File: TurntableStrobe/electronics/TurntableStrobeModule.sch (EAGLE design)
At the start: 11 parts, among them IC1 TINY25, J1 ISP, Q1 12MHz

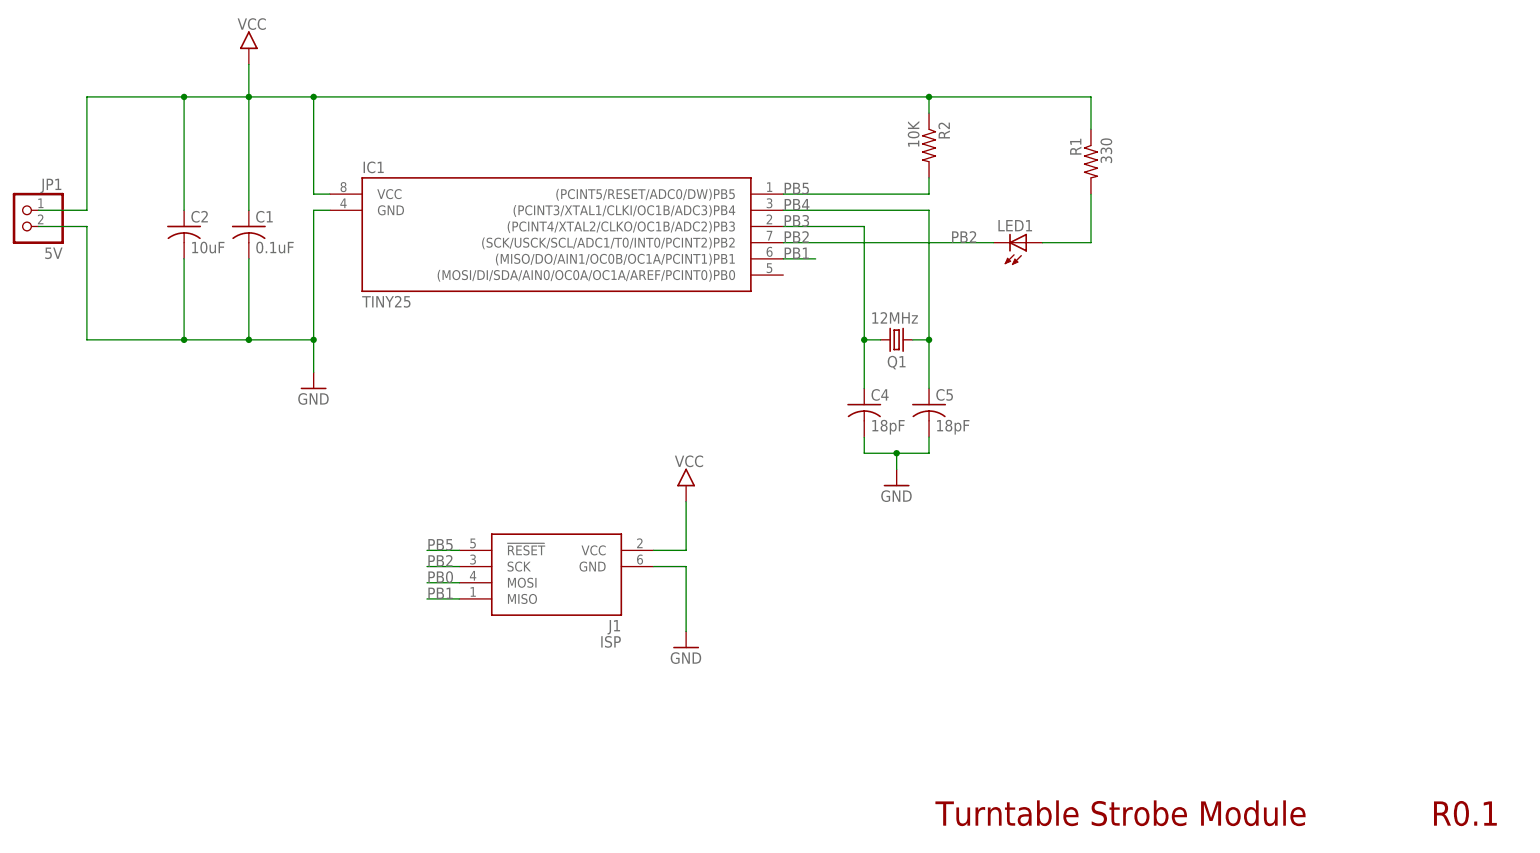
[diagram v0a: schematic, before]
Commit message: Fixed bug with missing MOSI.
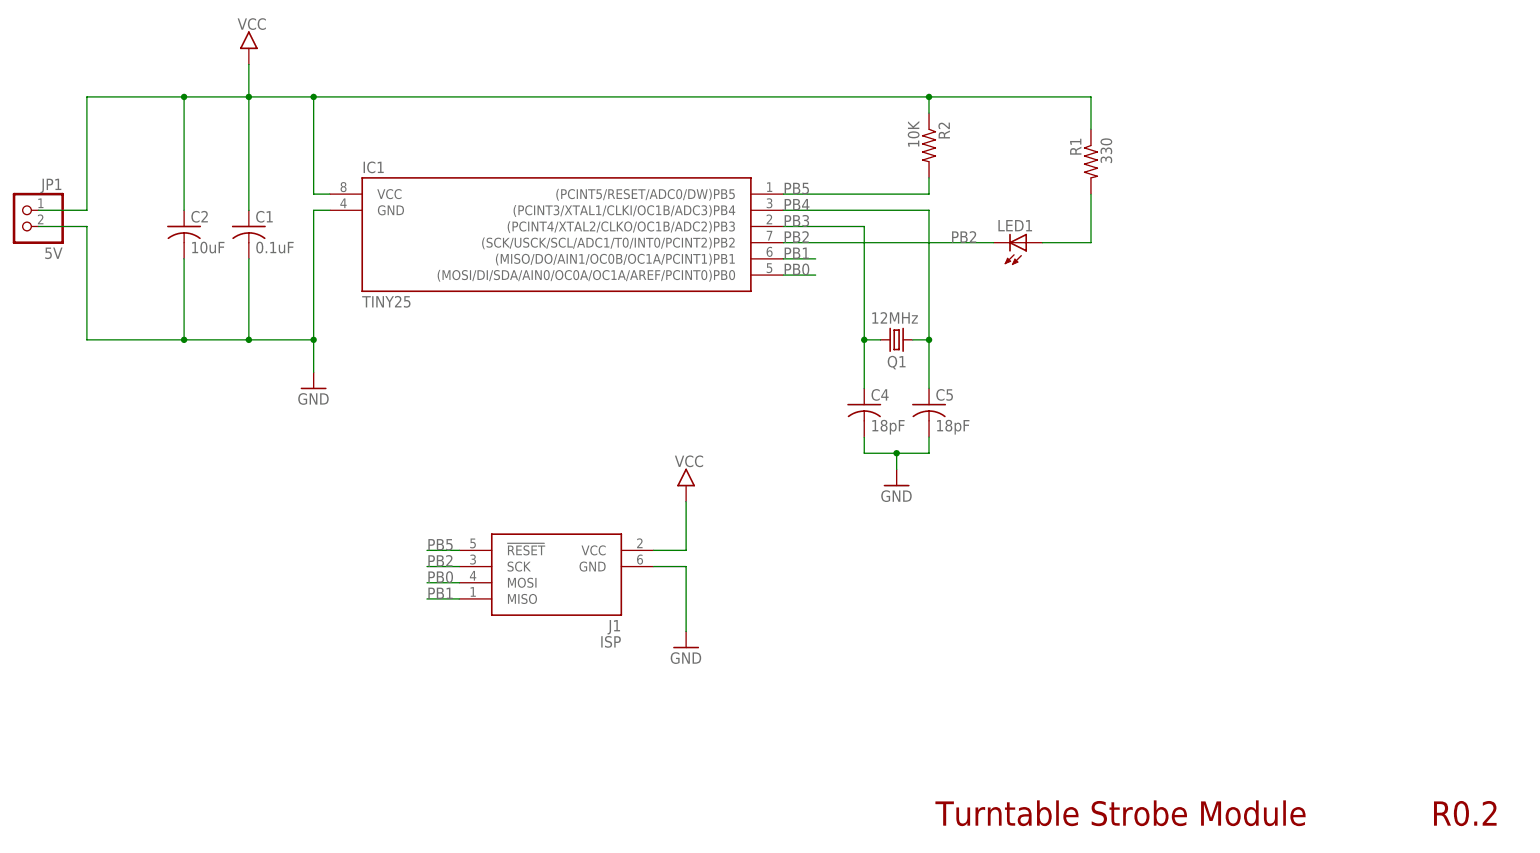
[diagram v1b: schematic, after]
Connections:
- net PB0: now also IC1.(MOSI/DI/SDA/AIN0/OC0A/OC1A/AREF/PCINT0)PB0
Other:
- note added: "R0.2"
- note removed: "R0.1"
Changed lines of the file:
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@@
 <grid distance="0.1" unitdist="inch" unit="inch" style="lines" multiple="1" display="no" altdistance="0.01" altunitdist="inch" altunit="inch"/>
 <layers>
-<layer number="1" name="Top" color="4" fill="1" visible="yes" active="no"/>
-<layer number="16" name="Bottom" color="1" fill="1" visible="yes" active="no"/>
-<layer number="17" name="Pads" color="2" fill="1" visible="yes" active="no"/>
-<layer number="18" name="Vias" color="2" fill="1" visible="yes" active="no"/>
-<layer number="19" name="Unrouted" color="6" fill="1" visible="yes" active="no"/>
-<layer number="20" name="Dimension" color="15" fill="1" visible="yes" active="no"/>
-<layer number="21" name="tPlace" color="7" fill="1" visible="yes" active="no"/>
-<layer number="22" name="bPlace" color="7" fill="1" visible="yes" active="no"/>
-<layer number="23" name="tOrigins" color="15" fill="1" visible="yes" active="no"/>
-<layer number="24" name="bOrigins" color="15" fill="1" visible="yes" active="no"/>
-<layer number="25" name="tNames" color="7" fill="1" visible="yes" active="no"/>
-<layer number="26" name="bNames" color="7" fill="1" visible="yes" active="no"/>
-<layer number="27" name="tValues" color="7" fill="1" visible="yes" active="no"/>
-<layer number="28" name="bValues" color="7" fill="1" visible="yes" active="no"/>
+<layer number="1" name="Top" color="4" fill="1" visible="no" active="no"/>
+<layer number="16" name="Bottom" color="1" fill="1" visible="no" active="no"/>
+<layer number="17" name="Pads" color="2" fill="1" visible="no" active="no"/>
+<layer number="18" name="Vias" color="2" fill="1" visible="no" active="no"/>
+<layer number="19" name="Unrouted" color="6" fill="1" visible="no" active="no"/>
+<layer number="20" name="Dimension" color="15" fill="1" visible="no" active="no"/>
+<layer number="21" name="tPlace" color="7" fill="1" visible="no" active="no"/>
+<layer number="22" name="bPlace" color="7" fill="1" visible="no" active="no"/>
+<layer number="23" name="tOrigins" color="15" fill="1" visible="no" active="no"/>
+<layer number="24" name="bOrigins" color="15" fill="1" visible="no" active="no"/>
+<layer number="25" name="tNames" color="7" fill="1" visible="no" active="no"/>
+<layer number="26" name="bNames" color="7" fill="1" visible="no" active="no"/>
+<layer number="27" name="tValues" color="7" fill="1" visible="no" active="no"/>
+<layer number="28" name="bValues" color="7" fill="1" visible="no" active="no"/>
 <layer number="29" name="tStop" color="7" fill="3" visible="no" active="no"/>
 <layer number="30" name="bStop" color="7" fill="6" visible="no" active="no"/>
@@
 <layer number="35" name="tGlue" color="7" fill="4" visible="no" active="no"/>
 <layer number="36" name="bGlue" color="7" fill="5" visible="no" active="no"/>
-<layer number="37" name="tTest" color="7" fill="1" visible="yes" active="no"/>
-<layer number="38" name="bTest" color="7" fill="1" visible="yes" active="no"/>
+<layer number="37" name="tTest" color="7" fill="1" visible="no" active="no"/>
+<layer number="38" name="bTest" color="7" fill="1" visible="no" active="no"/>
 <layer number="39" name="tKeepout" color="4" fill="11" visible="no" active="no"/>
 <layer number="40" name="bKeepout" color="1" fill="11" visible="no" active="no"/>
@@
 <layer number="44" name="Drills" color="7" fill="1" visible="no" active="no"/>
 <layer number="45" name="Holes" color="7" fill="1" visible="no" active="no"/>
-<layer number="46" name="Milling" color="3" fill="1" visible="yes" active="no"/>
-<layer number="47" name="Measures" color="7" fill="1" visible="yes" active="no"/>
-<layer number="48" name="Document" color="7" fill="1" visible="yes" active="no"/>
-<layer number="49" name="Reference" color="7" fill="1" visible="yes" active="no"/>
-<layer number="50" name="dxf" color="7" fill="1" visible="yes" active="no"/>
-<layer number="51" name="tDocu" color="7" fill="1" visible="yes" active="no"/>
-<layer number="52" name="bDocu" color="7" fill="1" visible="yes" active="no"/>
-<layer number="53" name="tPadExt" color="7" fill="1" visible="yes" active="no"/>
-<layer number="54" name="bPadExt" color="1" fill="1" visible="yes" active="no"/>
-<layer number="56" name="wert" color="7" fill="1" visible="yes" active="no"/>
+<layer number="46" name="Milling" color="3" fill="1" visible="no" active="no"/>
+<layer number="47" name="Measures" color="7" fill="1" visible="no" active="no"/>
+<layer number="48" name="Document" color="7" fill="1" visible="no" active="no"/>
+<layer number="49" name="Reference" color="7" fill="1" visible="no" active="no"/>
+<layer number="50" name="dxf" color="7" fill="1" visible="no" active="no"/>
+<layer number="51" name="tDocu" color="7" fill="1" visible="no" active="no"/>
+<layer number="52" name="bDocu" color="7" fill="1" visible="no" active="no"/>
+<layer number="53" name="tPadExt" color="7" fill="1" visible="no" active="no"/>
+<layer number="54" name="bPadExt" color="1" fill="1" visible="no" active="no"/>
+<layer number="56" name="wert" color="7" fill="1" visible="no" active="no"/>
 <layer number="91" name="Nets" color="2" fill="1" visible="yes" active="yes"/>
 <layer number="92" name="Busses" color="1" fill="1" visible="yes" active="yes"/>
@@
 <plain>
 <text x="138.176" y="-30.48" size="3.81" layer="94">Turntable Strobe Module</text>
-<text x="215.9" y="-30.48" size="3.81" layer="94">R0.1</text>
+<text x="215.9" y="-30.48" size="3.81" layer="94">R0.2</text>
 </plain>
 <instances>
@@
 <label x="58.42" y="7.62" size="1.778" layer="95"/>
 </segment>
-</net>
+<segment>
+<pinref part="IC1" gate="1" pin="(MOSI/DI/SDA/AIN0/OC0A/OC1A/AREF/PCINT0)PB0"/>
+<wire x1="114.3" y1="55.88" x2="119.38" y2="55.88" width="0.1524" layer="91"/>
+<label x="114.3" y="55.88" size="1.778" layer="95"/>
+</segment>
+</net>
